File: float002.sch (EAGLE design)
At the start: 36 parts, among them X2 USB-MICROB, Y1 16MHz

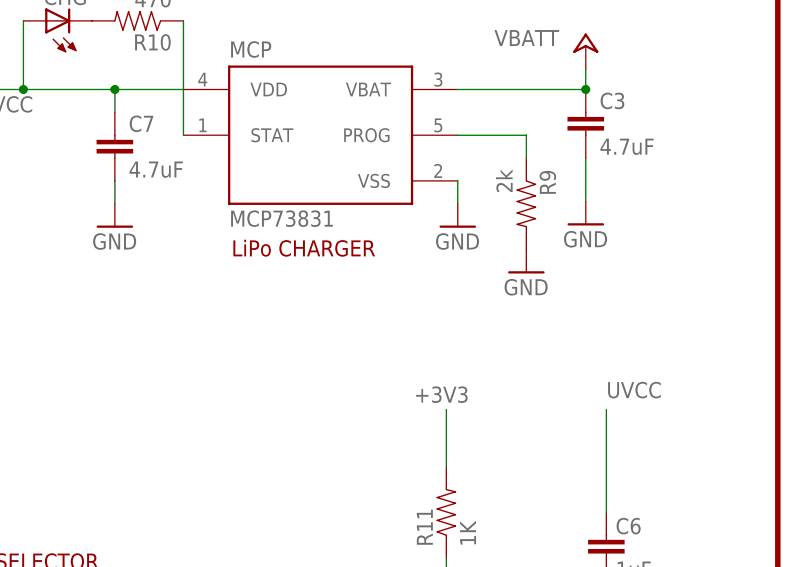
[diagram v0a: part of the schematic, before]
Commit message: added notes to schematic, BOM.txt
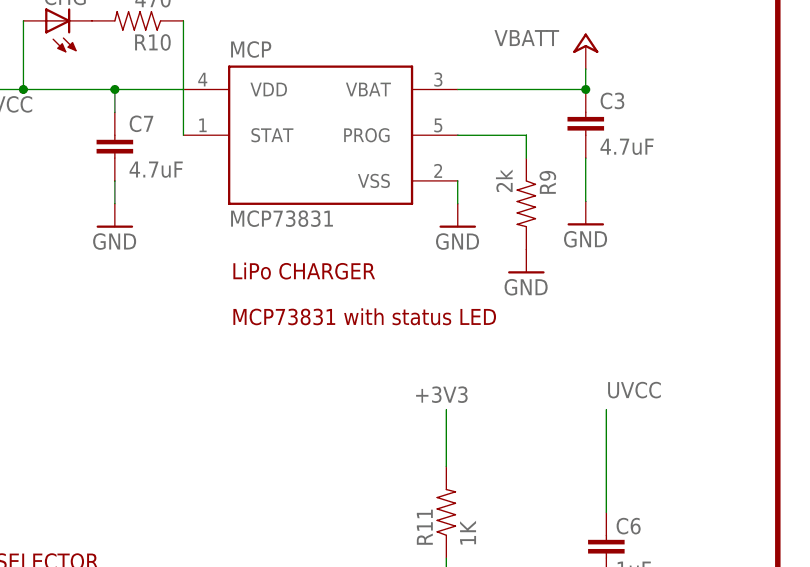
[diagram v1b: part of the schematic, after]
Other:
- note added: "MCP73831 with status LED"
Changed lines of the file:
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@@
 <text x="147.32" y="55.88" size="1.778" layer="94">BREAKOUT HEADER</text>
 <text x="161.29" y="120.65" size="1.778" layer="94">Bee socket</text>
-<text x="320.294" y="116.078" size="1.778" layer="94">LiPo CHARGER</text>
+<text x="320.294" y="113.538" size="1.778" layer="94">LiPo CHARGER</text>
 <text x="207.01" y="165.1" size="2.54" layer="94">POWER MANAGEMENT</text>
 <wire x1="200.66" y1="175.26" x2="200.66" y2="58.42" width="0.6096" layer="94"/>
@@
 <text x="266.7" y="35.56" size="1.778" layer="91">- need to check Fuse / decoupling capacitor placement </text>
 <text x="83.82" y="45.72" size="1.778" layer="91">- what about LED for RX; or WIFIDIN/DOUT?</text>
+<text x="320.294" y="108.458" size="1.778" layer="94">MCP73831 with status LED</text>
 </plain>
 <instances>

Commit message: more notes
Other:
- note added: "- UVCC always charges battery, powers 32u4"
- note removed: "- UVCC always charges battery"
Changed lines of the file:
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@@
 <setting verticaltext="up"/>
 </settings>
-<grid distance="50" unitdist="mil" unit="mil" style="lines" multiple="1" display="no" altdistance="0.01" altunitdist="inch" altunit="inch"/>
+<grid distance="0.1" unitdist="inch" unit="inch" style="lines" multiple="1" display="no" altdistance="0.01" altunitdist="inch" altunit="inch"/>
 <layers>
 <layer number="1" name="Top" color="4" fill="1" visible="no" active="no"/>
@@
 <text x="289.56" y="81.28" size="1.778" layer="94">VIN SELECTOR</text>
 <text x="298.45" y="66.04" size="1.6764" layer="94">UVCC-VIN</text>
-<text x="266.7" y="38.1" size="1.778" layer="91">- UVCC always charges battery</text>
+<text x="266.7" y="38.1" size="1.778" layer="91">- UVCC always charges battery, powers 32u4</text>
 <text x="266.7" y="40.64" size="1.778" layer="91">- VIN selector chooses who goes to Fuse then VREG (didn't want to connect UVCC and VBATT directly... better solution?</text>
 <text x="266.7" y="35.56" size="1.778" layer="91">- need to check Fuse / decoupling capacitor placement </text>
